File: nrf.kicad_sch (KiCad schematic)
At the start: 29 parts, among them U1 nRF52840, Y1 32MHz, Y2 32.768kHz

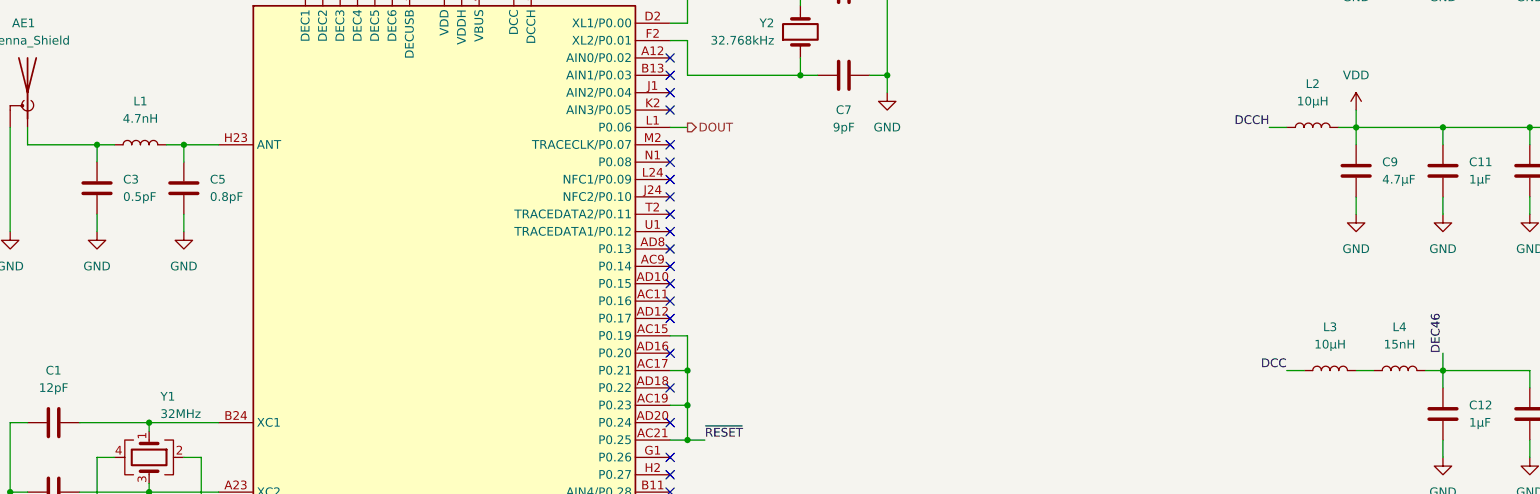
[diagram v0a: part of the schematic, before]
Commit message: Prepare for Aisler assembly
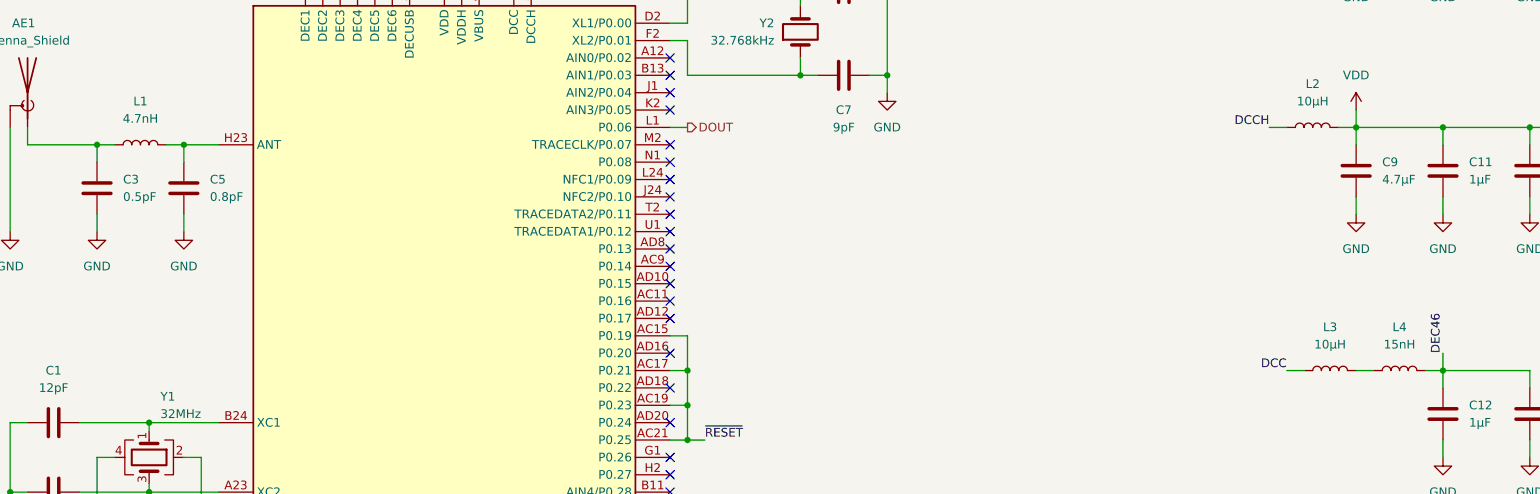
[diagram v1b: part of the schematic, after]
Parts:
- C1, C2: MFG (none) -> Murata Electronics; MPN (none) -> GRM1555C1H120FA01J; Mfr. Murata Electronics -> (none); Mfr. No GRM1555C1H120FA01J -> (none); Mouser No 81-GRM1555C1H120FA1J -> (none); Order Code (none) -> 81-GRM1555C1H120FA1J
- C10, C13, C8, C9: MFG (none) -> Murata Electronics; MPN (none) -> GRT188C71C475KE13D; Mfr. Murata Electronics -> (none); Mfr. No GRT188C71C475KE13D -> (none); Mouser No 81-GRT188C71C475KE13 -> (none); Order Code (none) -> 81-GRT188C71C475KE13
- C11, C12: MFG (none) -> Murata Electronics; MPN (none) -> GRT188R61H105KE13D; Mfr. Murata Electronics -> (none); Mfr. No GRT188R61H105KE13D -> (none); Mouser No 81-GRT188R61H105KE3D -> (none); Order Code (none) -> 81-GRT188R61H105KE3D
- C14, C16, C17, C19: MFG (none) -> Murata Electronics; MPN (none) -> GRM155R71A104KA01D; Mfr. Murata Electronics -> (none); Mfr. No GRM155R71A104KA01D -> (none); Mouser No 81-GRM155R71A104KA1D -> (none); Order Code (none) -> 81-GRM155R71A104KA1D
- C15: MFG (none) -> Murata Electronics; MPN (none) -> GRM155C71H473JE19D; Mfr. Murata Electronics -> (none); Mfr. No GRM155C71H473JE19D -> (none); Mouser No 81-GRM155C71H473JE9D -> (none); Order Code (none) -> 81-GRM155C71H473JE9D
- C18: MFG (none) -> Murata Electronics; MPN (none) -> GRM1555C1H101JA01D; Mfr. Murata Electronics -> (none); Mfr. No GRM1555C1H101JA01D -> (none); Mouser No 81-GRM1555C1H101JA1D -> (none); Order Code (none) -> 81-GRM1555C1H101JA1D
- C3: MFG (none) -> Murata Electronics; MPN (none) -> GJM1555C1HR50RB12D; Mfr. Murata Electronics -> (none); Mfr. No GJM1555C1HR50RB12D -> (none); Mouser No 81-GJM1555C1HR50RB2D -> (none); Order Code (none) -> 81-GJM1555C1HR50RB2D
- C5: MFG (none) -> Murata Electronics; MPN (none) -> GJM1555C1HR80WB01D; Mfr. Murata Electronics -> (none); Mfr. No GJM1555C1HR80WB01D -> (none); Mouser No 81-GJM1555C1HR80WB1D -> (none); Order Code (none) -> 81-GJM1555C1HR80WB1D
- C6, C7: MFG (none) -> Murata Electronics; MPN (none) -> GJM1555C1H9R0CB01J; Mfr. Murata Electronics -> (none); Mfr. No GJM1555C1H9R0CB01J -> (none); Mouser No 81-GJM1555C1H9R0CB1J -> (none); Order Code (none) -> 81-GJM1555C1H9R0CB1J
- L1: MFG (none) -> Murata Electronics; MPN (none) -> LQW15AN4N7B00D; Mfr. Murata Electronics -> (none); Mfr. No LQW15AN4N7B00D -> (none); Mouser No 81-LQW15AN4N7B00D -> (none); Order Code (none) -> 81-LQW15AN4N7B00D
- L2, L3: MFG (none) -> Murata Electronics; MPN (none) -> LQM18DZ100M70L; Mfr. Murata Electronics -> (none); Mfr. No LQM18DZ100M70L -> (none); Mouser No 81-LQM18DZ100M70L -> (none); Order Code (none) -> 81-LQM18DZ100M70L
- L4: MFG (none) -> Murata Electronics; MPN (none) -> LQG15HS15NG02D; Mfr. Murata Electronics -> (none); Mfr. No LQG15HS15NG02D -> (none); Mouser No 81-LQG15HS15NG02D -> (none); Order Code (none) -> 81-LQG15HS15NG02D
- R1: MFG (none) -> YAGEO; MPN (none) -> RC0402FR-0710KL; Mfr. YAGEO -> (none); Mfr. No RC0402FR-0710KL -> (none); Mouser No 603-RC0402FR-0710KL -> (none); Order Code (none) -> 603-RC0402FR-0710KL
- TP1, TP2: now left out of the parts list
- U1: MFG (none) -> Nordic Semiconductor; MPN (none) -> NRF52840-QIAA-R7; Mfr. Nordic Semiconductor -> (none); Mfr. No NRF52840-QIAA-R7 -> (none); Mouser No 949-NRF52840-QIAA-R7 -> (none); Order Code (none) -> 949-NRF52840-QIAA-R7
- Y1: MFG (none) -> ABRACON; MPN (none) -> ABM11W-32.0000MHZ-8-D1X-T3; Mfr. ABRACON -> (none); Mfr. No ABM11W-32.0000MHZ-8-D1X-T3 -> (none); Mouser No 815-11W32-8D1XT -> (none); Order Code (none) -> 815-11W32-8D1XT
- Y2: MFG (none) -> ABRACON; MPN (none) -> ABS07-32.768KHZ-7-T; Mfr. ABRACON -> (none); Mfr. No ABS07-32.768KHZ-7-T -> (none); Mouser No 815-ABS07-32.768K7T -> (none); Order Code (none) -> 815-ABS07-32.768K7T
